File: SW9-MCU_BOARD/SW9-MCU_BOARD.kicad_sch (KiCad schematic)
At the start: 20 parts, among them IC1 STM32L051C6T6, J1 Conn_ARM_JTAG_SWD_10, SW1 SW_DPDT_x2, SW2 SW_Push, Y1 32KHz, Y2 8MHz

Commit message: update stuff
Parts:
- C1, C10, C11, C2, C3, C4, C5, C6, C7, C8, C9: footprint (none) -> Capacitor_SMD:C_0603_1608Metric_Pad1.08x0.95mm_HandSolder
- FB1: footprint (none) -> Ferrite_THT:LairdTech_28C0236-0JW-10
- IC1: footprint QFP50P900X900X160-48N -> SWLib:QFP50P900X900X160-48N
- J1: footprint (none) -> Connector_PinSocket_2.00mm:PinSocket_1x10_P2.00mm_Vertical
- R1, R2: footprint (none) -> Resistor_SMD:R_0603_1608Metric_Pad0.98x0.95mm_HandSolder
- SW1: footprint (none) -> Button_Switch_SMD:SW_DPDT_CK_JS202011JCQN
- SW2: footprint (none) -> Button_Switch_THT:SW_Push_2P2T_Toggle_CK_PVA2OAH5xxxxxxV2
- Y1: footprint (none) -> SWLib:X_ABS25_ABR
- Y2: footprint (none) -> SWLib:830003151
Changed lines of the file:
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@@
       (effects (font (size 1.27 1.27)))
     )
-    (property "Footprint" "" (at 149.86 26.67 0)
+    (property "Footprint" "Button_Switch_SMD:SW_DPDT_CK_JS202011JCQN" (at 149.86 26.67 0)
       (effects (font (size 1.27 1.27)) hide)
     )
@@
       (effects (font (size 1.27 1.27)) (justify left))
     )
-    (property "Footprint" "" (at 256.2352 134.62 0)
+    (property "Footprint" "Capacitor_SMD:C_0603_1608Metric_Pad1.08x0.95mm_HandSolder" (at 256.2352 134.62 0)
       (effects (font (size 1.27 1.27)) hide)
     )
@@
       (effects (font (size 1.27 1.27)) (justify left))
     )
-    (property "Footprint" "" (at 240.9952 134.62 0)
+    (property "Footprint" "Capacitor_SMD:C_0603_1608Metric_Pad1.08x0.95mm_HandSolder" (at 240.9952 134.62 0)
       (effects (font (size 1.27 1.27)) hide)
     )
@@
       (effects (font (size 1.27 1.27)) (justify left))
     )
-    (property "Footprint" "" (at 185.1152 134.62 0)
+    (property "Footprint" "Capacitor_SMD:C_0603_1608Metric_Pad1.08x0.95mm_HandSolder" (at 185.1152 134.62 0)
       (effects (font (size 1.27 1.27)) hide)
     )
@@
       (effects (font (size 1.27 1.27)))
     )
-    (property "Footprint" "QFP50P900X900X160-48N" (at 170.18 62.9219 0)
+    (property "Footprint" "SWLib:QFP50P900X900X160-48N" (at 170.18 62.9219 0)
       (effects (font (size 1.27 1.27)))
     )
@@
       (effects (font (size 1.27 1.27)) (justify left))
     )
-    (property "Footprint" "" (at 227.0252 134.62 0)
+    (property "Footprint" "Capacitor_SMD:C_0603_1608Metric_Pad1.08x0.95mm_HandSolder" (at 227.0252 134.62 0)
       (effects (font (size 1.27 1.27)) hide)
     )
@@
       (effects (font (size 1.27 1.27)))
     )
-    (property "Footprint" "" (at 93.98 96.52 0)
+    (property "Footprint" "SWLib:X_ABS25_ABR" (at 93.98 96.52 0)
       (effects (font (size 1.27 1.27)) hide)
     )
@@
       (effects (font (size 1.27 1.27)) (justify left))
     )
-    (property "Footprint" "" (at 78.4352 93.98 0)
+    (property "Footprint" "Capacitor_SMD:C_0603_1608Metric_Pad1.08x0.95mm_HandSolder" (at 78.4352 93.98 0)
       (effects (font (size 1.27 1.27)) hide)
     )
@@
       (effects (font (size 1.27 1.27)))
     )
-    (property "Footprint" "" (at 198.12 122.682 90)
+    (property "Footprint" "Ferrite_THT:LairdTech_28C0236-0JW-10" (at 198.12 122.682 90)
       (effects (font (size 1.27 1.27)) hide)
     )
@@
       (effects (font (size 1.27 1.27)) (justify left))
     )
-    (property "Footprint" "" (at 171.1452 134.62 0)
+    (property "Footprint" "Capacitor_SMD:C_0603_1608Metric_Pad1.08x0.95mm_HandSolder" (at 171.1452 134.62 0)
       (effects (font (size 1.27 1.27)) hide)
     )
@@
       (effects (font (size 1.27 1.27)))
     )
-    (property "Footprint" "" (at 128.27 135.89 0)
+    (property "Footprint" "Button_Switch_THT:SW_Push_2P2T_Toggle_CK_PVA2OAH5xxxxxxV2" (at 128.27 135.89 0)
       (effects (font (size 1.27 1.27)) hide)
     )
@@
       (effects (font (size 1.27 1.27)))
     )
-    (property "Footprint" "" (at 139.954 25.654 90)
+    (property "Footprint" "Resistor_SMD:R_0603_1608Metric_Pad0.98x0.95mm_HandSolder" (at 139.954 25.654 90)
       (effects (font (size 1.27 1.27)) hide)
     )
@@
       (effects (font (size 1.27 1.27)) (justify right))
     )
-    (property "Footprint" "" (at 74.93 148.59 0)
+    (property "Footprint" "Connector_PinSocket_2.00mm:PinSocket_1x10_P2.00mm_Vertical" (at 74.93 148.59 0)
       (effects (font (size 1.27 1.27)) hide)
     )
@@
       (effects (font (size 1.27 1.27)))
     )
-    (property "Footprint" "" (at 69.85 83.82 0)
+    (property "Footprint" "SWLib:830003151" (at 69.85 83.82 0)
       (effects (font (size 1.27 1.27)) hide)
     )
@@
       (effects (font (size 1.27 1.27)))
     )
-    (property "Footprint" "" (at 132.08 150.1648 0)
+    (property "Footprint" "Capacitor_SMD:C_0603_1608Metric_Pad1.08x0.95mm_HandSolder" (at 132.08 150.1648 0)
       (effects (font (size 1.27 1.27)) hide)
     )
@@
       (effects (font (size 1.27 1.27)) (justify left))
     )
-    (property "Footprint" "" (at 100.0252 114.3 0)
+    (property "Footprint" "Capacitor_SMD:C_0603_1608Metric_Pad1.08x0.95mm_HandSolder" (at 100.0252 114.3 0)
       (effects (font (size 1.27 1.27)) hide)
     )
@@
       (effects (font (size 1.27 1.27)) (justify left))
     )
-    (property "Footprint" "" (at 88.5952 114.3 0)
+    (property "Footprint" "Capacitor_SMD:C_0603_1608Metric_Pad1.08x0.95mm_HandSolder" (at 88.5952 114.3 0)
       (effects (font (size 1.27 1.27)) hide)
     )
@@
       (effects (font (size 1.27 1.27)) (justify left))
     )
-    (property "Footprint" "" (at 100.076 101.854 90)
+    (property "Footprint" "Resistor_SMD:R_0603_1608Metric_Pad0.98x0.95mm_HandSolder" (at 100.076 101.854 90)
       (effects (font (size 1.27 1.27)) hide)
     )
@@
       (effects (font (size 1.27 1.27)) (justify left))
     )
-    (property "Footprint" "" (at 211.7852 134.62 0)
+    (property "Footprint" "Capacitor_SMD:C_0603_1608Metric_Pad1.08x0.95mm_HandSolder" (at 211.7852 134.62 0)
       (effects (font (size 1.27 1.27)) hide)
     )
@@
       (effects (font (size 1.27 1.27)) (justify left))
     )
-    (property "Footprint" "" (at 61.9252 93.98 0)
-      (effects (font (size 1.27 1.27)) hide)
-    )
+    (property "Footprint" "Capacitor_SMD:C_0603_1608Metric_Pad1.08x0.95mm_HandSolder" (at 61.9252 93.98 0)
+      (effects (font (size 1.27 1.27)) hide)
+    )

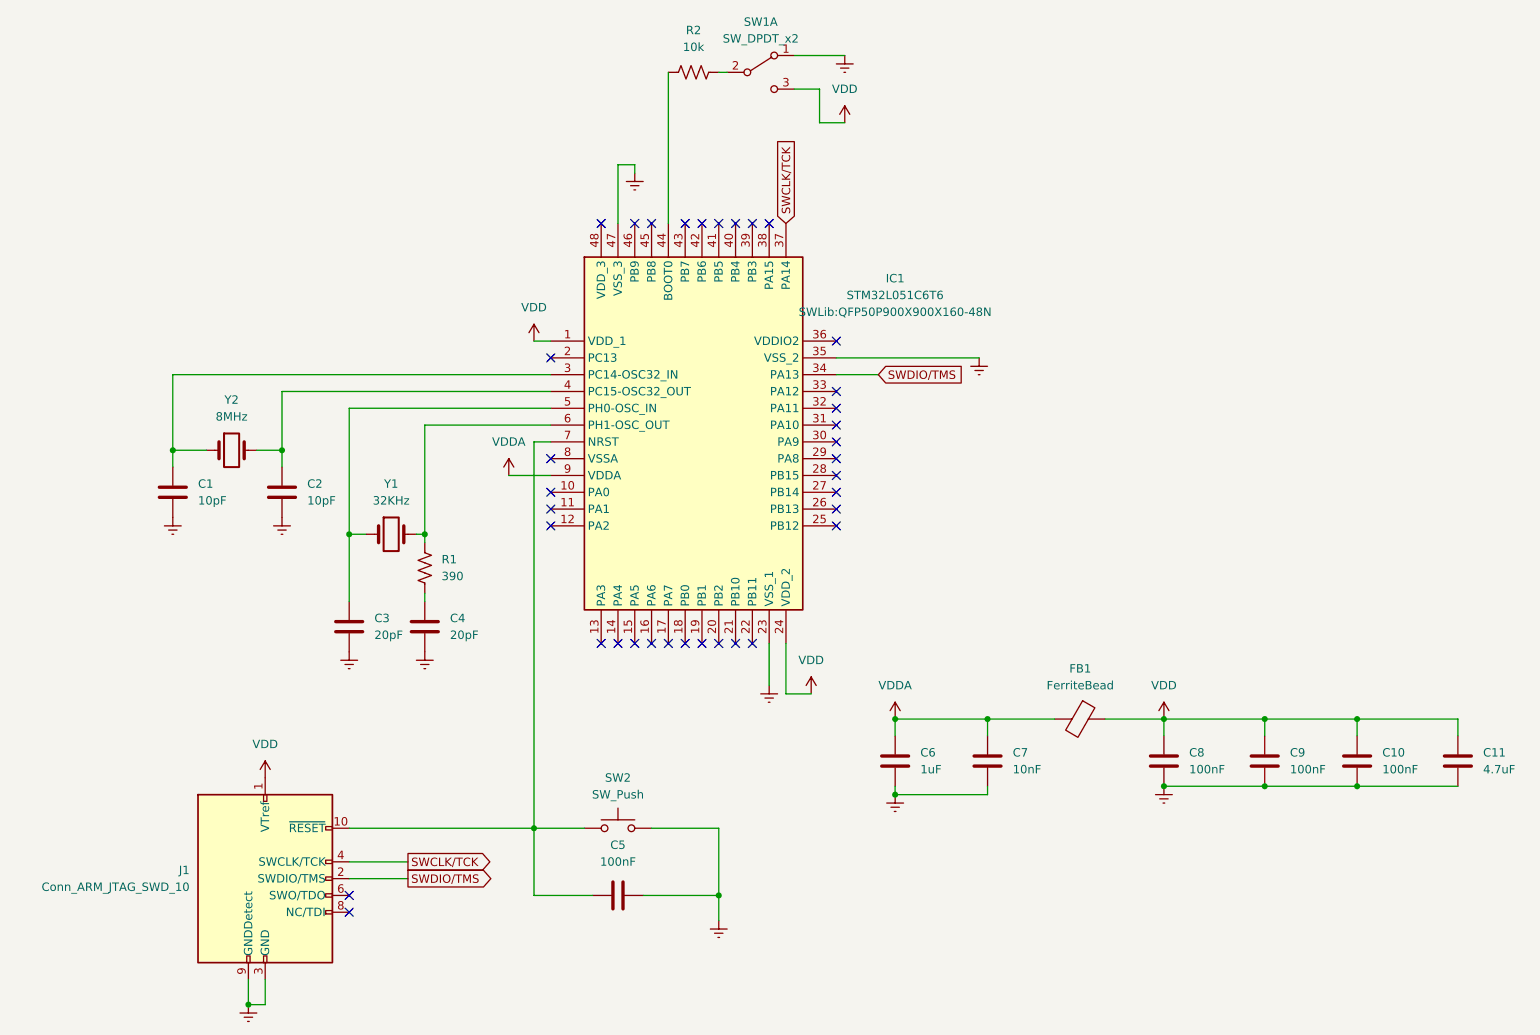
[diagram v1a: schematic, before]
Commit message: change footprints for oscillators
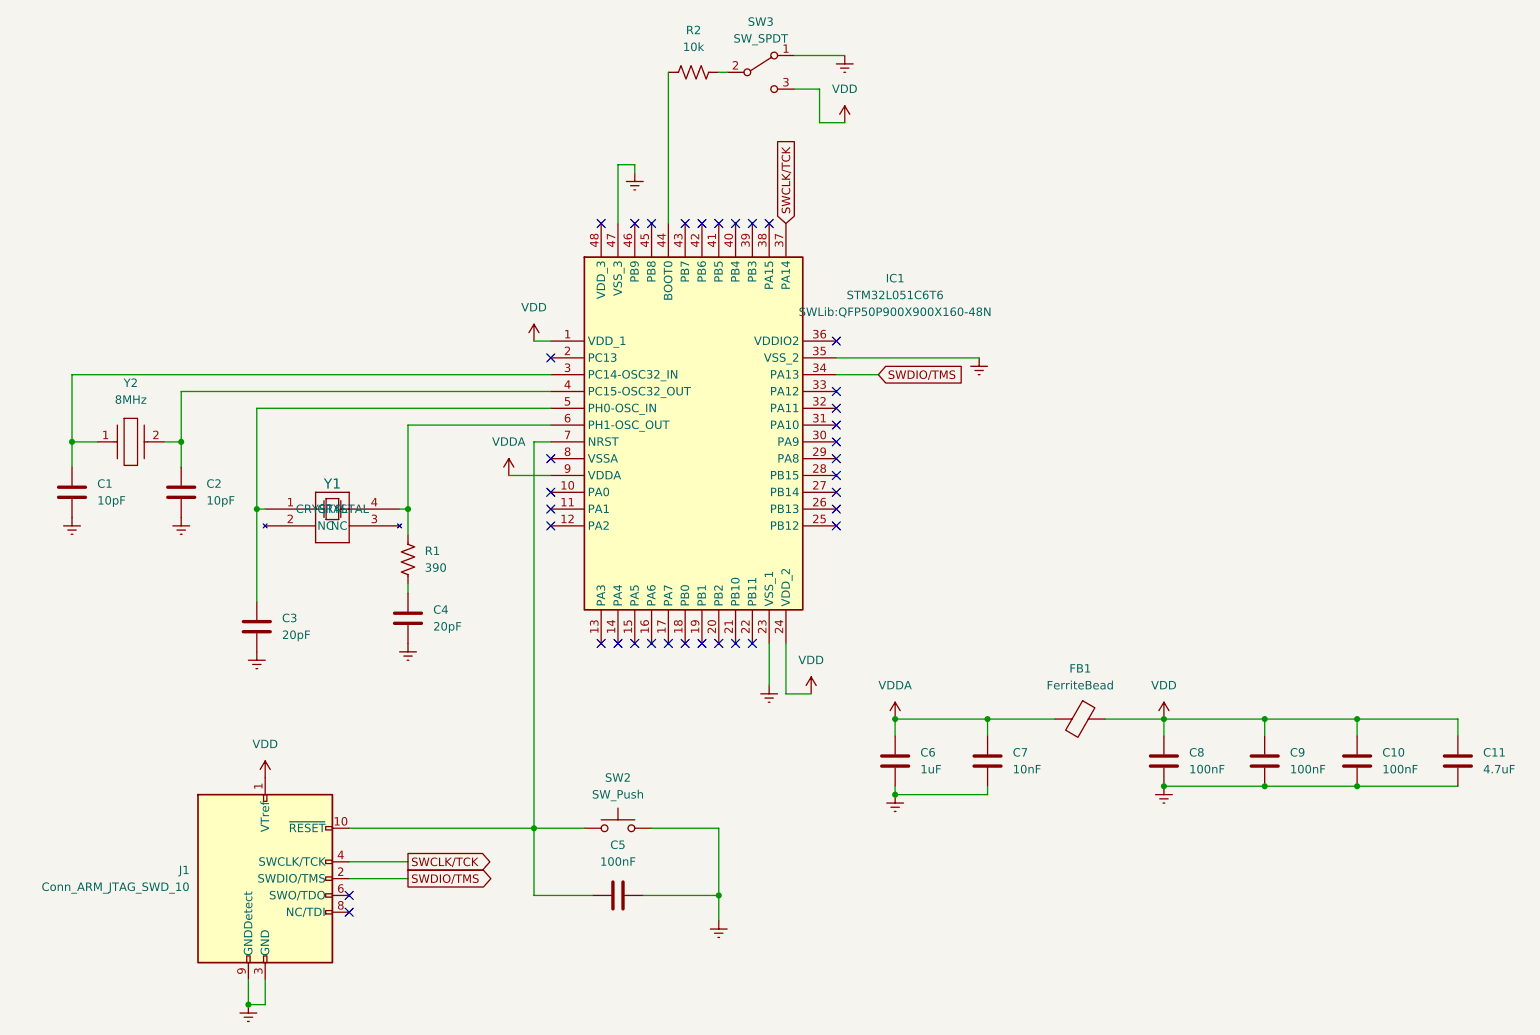
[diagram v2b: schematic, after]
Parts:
- removed SW1: SW_DPDT_x2, Button_Switch_SMD:SW_DPDT_CK_JS202011JCQN, symbol Switch:SW_DPDT_x2
- removed Y1: 32KHz, SWLib:X_ABS25_ABR, symbol Device:Crystal
- removed Y2: 8MHz, SWLib:830003151, symbol Device:Crystal
- added SW3: SW_SPDT, Button_Switch_SMD:SW_SPDT_PCM12, symbol Switch:SW_SPDT
- added Y1: ABS25-32.768KHZ-6-T, SWLib:X_ABS25_ABR, symbol SWLib:ABS25-32.768KHZ-6-T
- added Y2: 8MHz, SWLib:830003151, symbol SWLib:830003151
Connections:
- net Earth: now also SW3.1 (A)
- net VDD: now also SW3.3 (C)
- net at R2.2: now also SW3.2 (B)
- net at C1.1, IC1.3 (PC14-OSC32_IN): now also Y2.1
- net at C2.1, IC1.4 (PC15-OSC32_OUT): now also Y2.2
- net at C3.1, IC1.5 (PH0-OSC_IN): now also Y1.1 (CRYSTAL)
- net at IC1.6 (PH1-OSC_OUT), R1.1: now also Y1.4 (CRYSTAL)
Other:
- moved on the sheet: C1, C2, C3, C4, R1

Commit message: some changes ig???
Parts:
- FB1: footprint Ferrite_THT:LairdTech_28C0236-0JW-10 -> Inductor_SMD:L_0201_0603Metric_Pad0.64x0.40mm_HandSolder
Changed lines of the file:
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@@
       (effects (font (size 1.27 1.27)))
     )
-    (property "Footprint" "Ferrite_THT:LairdTech_28C0236-0JW-10" (at 198.12 122.682 90)
+    (property "Footprint" "Inductor_SMD:L_0201_0603Metric_Pad0.64x0.40mm_HandSolder" (at 198.12 122.682 90)
       (effects (font (size 1.27 1.27)) hide)
     )

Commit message: more routing
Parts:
- removed C10: 100nF, Capacitor_SMD:C_0603_1608Metric_Pad1.08x0.95mm_HandSolder, symbol Device:C
- renumbered C11 to C10
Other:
- moved on the sheet: C10
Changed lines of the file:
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@@
   (junction (at 170.18 124.46) (diameter 0) (color 0 0 0 0)
   )
-  (junction (at 240.03 124.46) (diameter 0) (color 0 0 0 0)
-  )
   (junction (at 226.06 134.62) (diameter 0) (color 0 0 0 0)
   )
@@
   )
   (junction (at 184.15 124.46) (diameter 0) (color 0 0 0 0)
-  )
-  (junction (at 240.03 134.62) (diameter 0) (color 0 0 0 0)
   )
   (junction (at 96.52 92.71) (diameter 0) (color 0 0 0 0)
@@
     (stroke (width 0) (type default))
   )
-  (wire (pts (xy 240.03 124.46) (xy 240.03 127))
-    (stroke (width 0) (type default))
-  )
   (wire (pts (xy 161.29 72.39) (xy 167.64 72.39))
     (stroke (width 0) (type default))
@@
     (stroke (width 0) (type default))
   )
-  (wire (pts (xy 226.06 134.62) (xy 240.03 134.62))
-    (stroke (width 0) (type default))
-  )
   (wire (pts (xy 201.93 124.46) (xy 210.82 124.46))
     (stroke (width 0) (type default))
@@
     (stroke (width 0) (type default))
   )
-  (wire (pts (xy 240.03 124.46) (xy 255.27 124.46))
-    (stroke (width 0) (type default))
-  )
   (wire (pts (xy 226.06 124.46) (xy 226.06 127))
     (stroke (width 0) (type default))
@@
     (stroke (width 0) (type default))
   )
-  (wire (pts (xy 240.03 134.62) (xy 255.27 134.62))
+  (wire (pts (xy 226.06 134.62) (xy 241.3 134.62))
     (stroke (width 0) (type default))
   )
@@
     (stroke (width 0) (type default))
   )
-  (wire (pts (xy 255.27 124.46) (xy 255.27 127))
+  (wire (pts (xy 241.3 124.46) (xy 241.3 127))
     (stroke (width 0) (type default))
   )
@@
     (stroke (width 0) (type default))
   )
-  (wire (pts (xy 226.06 124.46) (xy 240.03 124.46))
+  (wire (pts (xy 226.06 124.46) (xy 241.3 124.46))
     (stroke (width 0) (type default))
   )
@@
     )
   )
-  (symbol (lib_id "Device:C") (at 255.27 130.81 0) (unit 1)
+  (symbol (lib_id "Device:C") (at 241.3 130.81 0) (unit 1)
     (in_bom yes) (on_board yes) (dnp no) (fields_autoplaced)
-    (property "Reference" "C11" (at 259.08 129.54 0)
+    (property "Reference" "C10" (at 245.11 129.54 0)
       (effects (font (size 1.27 1.27)) (justify left))
     )
-    (property "Value" "4.7uF" (at 259.08 132.08 0)
+    (property "Value" "4.7uF" (at 245.11 132.08 0)
       (effects (font (size 1.27 1.27)) (justify left))
     )
-    (property "Footprint" "Capacitor_SMD:C_0603_1608Metric_Pad1.08x0.95mm_HandSolder" (at 256.2352 134.62 0)
-      (effects (font (size 1.27 1.27)) hide)
-    )
-    (property "Datasheet" "~" (at 255.27 130.81 0)
-      (effects (font (size 1.27 1.27)) hide)
-    )
-    (pin "2")
-    (pin "1")
-    (instances
-      (project "SW9-MCU_BOARD"
-        (path "/98be697d-8cf2-4efe-bafa-8172d9e478e0"
-          (reference "C11") (unit 1)
-        )
-      )
-    )
-  )
-  (symbol (lib_id "Device:C") (at 240.03 130.81 0) (unit 1)
-    (in_bom yes) (on_board yes) (dnp no) (fields_autoplaced)
-    (property "Reference" "C10" (at 243.84 129.54 0)
-      (effects (font (size 1.27 1.27)) (justify left))
-    )
-    (property "Value" "100nF" (at 243.84 132.08 0)
-      (effects (font (size 1.27 1.27)) (justify left))
-    )
-    (property "Footprint" "Capacitor_SMD:C_0603_1608Metric_Pad1.08x0.95mm_HandSolder" (at 240.9952 134.62 0)
-      (effects (font (size 1.27 1.27)) hide)
-    )
-    (property "Datasheet" "~" (at 240.03 130.81 0)
-      (effects (font (size 1.27 1.27)) hide)
-    )
+    (property "Footprint" "Capacitor_SMD:C_0603_1608Metric_Pad1.08x0.95mm_HandSolder" (at 242.2652 134.62 0)
+      (effects (font (size 1.27 1.27)) hide)
+    )
+    (property "Datasheet" "~" (at 241.3 130.81 0)
+      (effects (font (size 1.27 1.27)) hide)
+    )

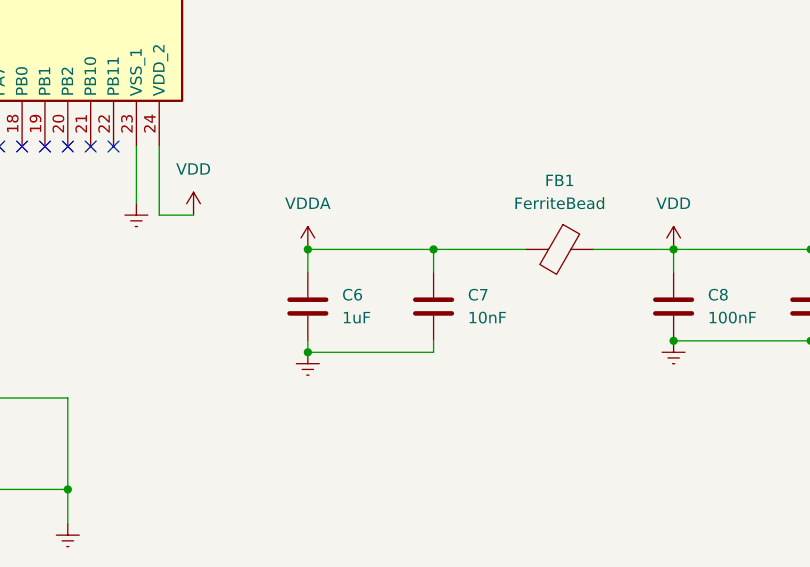
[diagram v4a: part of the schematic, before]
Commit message: change earth to gnd
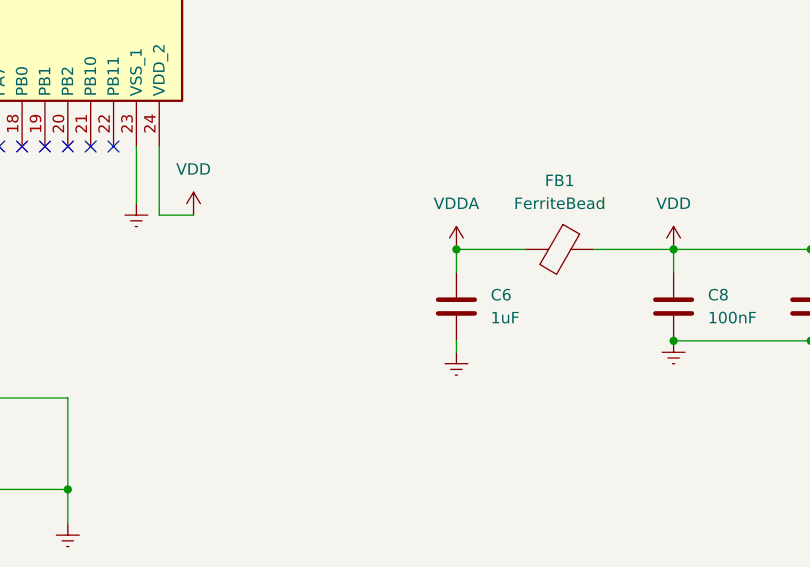
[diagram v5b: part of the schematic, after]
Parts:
- removed C7: 10nF, Capacitor_SMD:C_0603_1608Metric_Pad1.08x0.95mm_HandSolder, symbol Device:C
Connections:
- net Earth renamed GND
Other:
- moved on the sheet: C6
